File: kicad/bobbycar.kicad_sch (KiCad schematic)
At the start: 52 parts, among them J10 BREMSE, J11 CAN2, J12 PROG, J13 LED, J2 IO2, J3 GAS, J4 TFT, J5 Conn_02x08_Odd_Even, J6 Conn_02x08_Odd_Even, J7 BREMSE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

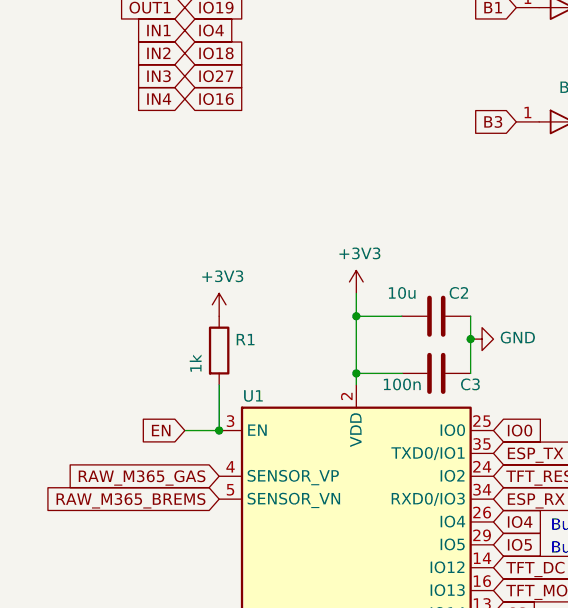
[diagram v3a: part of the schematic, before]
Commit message: Add capacitor to GND on EN
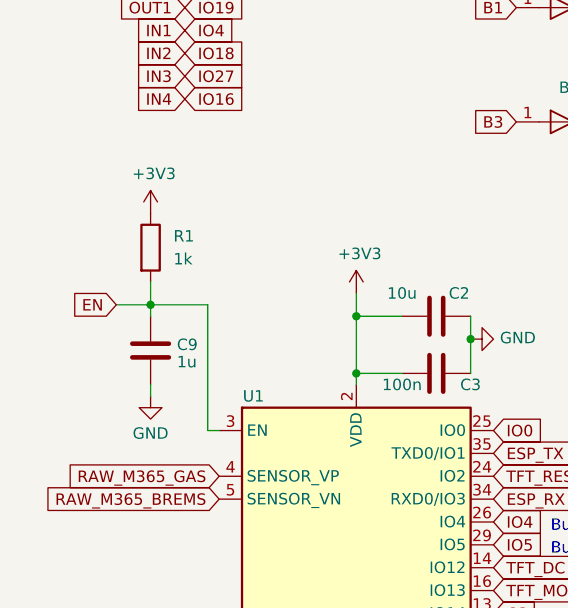
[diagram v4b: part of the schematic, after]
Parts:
- added C9: 1u, Capacitor_SMD:C_0805_2012Metric, symbol Device:C
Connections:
- net EN: now also C9.2
- net GND: now also C9.1
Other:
- moved on the sheet: R1
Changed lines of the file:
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@@
   (junction (at 109.22 170.18) (diameter 0) (color 0 0 0 0)
   )
+  (junction (at 27.94 54.61) (diameter 0) (color 0 0 0 0)
+  )
   (junction (at 350.52 102.87) (diameter 0) (color 0 0 0 0)
   )
@@
   (junction (at 115.57 39.37) (diameter 0) (color 0 0 0 0)
   )
-  (junction (at 35.56 68.58) (diameter 0) (color 0 0 0 0)
-  )
   (junction (at 391.16 95.25) (diameter 0) (color 0 0 0 0)
   )
@@
     (stroke (width 0) (type default))
   )
+  (wire (pts (xy 34.29 54.61) (xy 34.29 68.58))
+    (stroke (width 0) (type default))
+  )
   (wire (pts (xy 63.5 58.42) (xy 63.5 55.88))
     (stroke (width 0) (type default))
@@
     (stroke (width 0) (type default))
   )
+  (wire (pts (xy 34.29 68.58) (xy 35.56 68.58))
+    (stroke (width 0) (type default))
+  )
   (wire (pts (xy 120.65 170.18) (xy 109.22 170.18))
     (stroke (width 0) (type default))
@@
     (stroke (width 0) (type default))
   )
+  (wire (pts (xy 27.94 54.61) (xy 34.29 54.61))
+    (stroke (width 0) (type default))
+  )
   (wire (pts (xy 55.88 62.23) (xy 50.8 62.23))
     (stroke (width 0) (type default))
   )
+  (wire (pts (xy 27.94 63.5) (xy 27.94 64.77))
+    (stroke (width 0) (type default))
+  )
   (wire (pts (xy 161.29 107.95) (xy 156.21 107.95))
     (stroke (width 0) (type default))
   )
-  (wire (pts (xy 31.75 68.58) (xy 35.56 68.58))
+  (wire (pts (xy 24.13 54.61) (xy 27.94 54.61))
     (stroke (width 0) (type default))
   )
@@
     (stroke (width 0) (type default))
   )
+  (wire (pts (xy 27.94 54.61) (xy 27.94 55.88))
+    (stroke (width 0) (type default))
+  )
   (wire (pts (xy 57.15 182.88) (xy 72.39 182.88))
     (stroke (width 0) (type default))
   )
-  (wire (pts (xy 35.56 68.58) (xy 35.56 63.5))
+  (wire (pts (xy 27.94 54.61) (xy 27.94 52.07))
     (stroke (width 0) (type default))
   )
@@
     )
   )
-  (global_label "EN" (shape input) (at 31.75 68.58 180) (fields_autoplaced)
+  (global_label "EN" (shape input) (at 24.13 54.61 180) (fields_autoplaced)
     (effects (font (size 1.27 1.27)) (justify right))
-    (property "Intersheetrefs" "${INTERSHEET_REFS}" (at 0 0 0)
+    (property "Intersheetrefs" "${INTERSHEET_REFS}" (at -7.62 -13.97 0)
       (effects (font (size 1.27 1.27)) hide)
     )
-    (property "Referenzen zwischen Schaltplänen" "${INTERSHEET_REFS}" (at 0 0 0)
+    (property "Referenzen zwischen Schaltplänen" "${INTERSHEET_REFS}" (at -7.62 -13.97 0)
       (effects (font (size 1.27 1.27)) hide)
     )
@@
     )
   )
-  (symbol (lib_id "Device:R") (at 35.56 59.69 0) (unit 1)
+  (symbol (lib_id "Device:R") (at 27.94 48.26 0) (unit 1)
     (in_bom yes) (on_board yes) (dnp no)
-    (property "Reference" "R1" (at 37.338 58.5216 0)
+    (property "Reference" "R1" (at 30.48 46.99 0)
       (effects (font (size 1.27 1.27)) (justify left))
     )
-    (property "Value" "1k" (at 33.02 62.23 90)
+    (property "Value" "1k" (at 30.48 49.53 0)
       (effects (font (size 1.27 1.27)) (justify left))
     )
-    (property "Footprint" "Resistor_SMD:R_0603_1608Metric" (at 33.782 59.69 90)
+    (property "Footprint" "Resistor_SMD:R_0603_1608Metric" (at 26.162 48.26 90)
       (effects (font (size 1.27 1.27)) hide)
     )
-    (property "Datasheet" "~" (at 35.56 59.69 0)
+    (property "Datasheet" "~" (at 27.94 48.26 0)
       (effects (font (size 1.27 1.27)) hide)
     )
-    (property "LCSC Part #" "C21190" (at 35.56 59.69 0)
+    (property "LCSC Part #" "C21190" (at 27.94 48.26 0)
       (effects (font (size 1.27 1.27)) hide)
     )
@@
     )
   )
-  (symbol (lib_id "power:+3V3") (at 35.56 55.88 0) (unit 1)
+  (symbol (lib_id "power:+3V3") (at 27.94 44.45 0) (unit 1)
     (in_bom yes) (on_board yes) (dnp no)
-    (property "Reference" "#PWR01" (at 35.56 59.69 0)
+    (property "Reference" "#PWR01" (at 27.94 48.26 0)
       (effects (font (size 1.27 1.27)) hide)
     )
-    (property "Value" "+3V3" (at 35.941 51.4858 0)
+    (property "Value" "+3V3" (at 28.321 40.0558 0)
       (effects (font (size 1.27 1.27)))
     )
-    (property "Footprint" "" (at 35.56 55.88 0)
+    (property "Footprint" "" (at 27.94 44.45 0)
       (effects (font (size 1.27 1.27)) hide)
     )
-    (property "Datasheet" "" (at 35.56 55.88 0)
+    (property "Datasheet" "" (at 27.94 44.45 0)
       (effects (font (size 1.27 1.27)) hide)
     )
@@
     )
   )
+  (symbol (lib_id "power:GND") (at 27.94 64.77 0) (unit 1)
+    (in_bom yes) (on_board yes) (dnp no) (fields_autoplaced)
+    (property "Reference" "#PWR023" (at 27.94 71.12 0)
+      (effects (font (size 1.27 1.27)) hide)
+    )
+    (property "Value" "GND" (at 27.94 68.9055 0)
+      (effects (font (size 1.27 1.27)))
+    )
+    (property "Footprint" "" (at 27.94 64.77 0)
+      (effects (font (size 1.27 1.27)) hide)
+    )
+    (property "Datasheet" "" (at 27.94 64.77 0)
+      (effects (font (size 1.27 1.27)) hide)
+    )
+    (pin "1")
+    (instances
+      (project "bobbycar"
+        (path "/477311b9-8f81-40c8-9c55-fd87e287247a"
+          (reference "#PWR023") (unit 1)
+        )
+      )
+    )
+  )
   (symbol (lib_id "power:GND") (at 212.09 -48.26 0) (unit 1)
     (in_bom yes) (on_board yes) (dnp no)
@@
         )
       )
+    )
+  )
+  (symbol (lib_id "Device:C") (at 27.94 59.69 180) (unit 1)
+    (in_bom yes) (on_board yes) (dnp no) (fields_autoplaced)
+    (property "Reference" "C9" (at 30.861 59.0463 0)
+      (effects (font (size 1.27 1.27)) (justify right))
+    )
+    (property "Value" "1u" (at 30.861 60.9673 0)
+      (effects (font (size 1.27 1.27)) (justify right))
+    )
+    (property "Footprint" "Capacitor_SMD:C_0805_2012Metric" (at 26.9748 55.88 0)
+      (effects (font (size 1.27 1.27)) hide)
+    )
+    (property "Datasheet" "~" (at 27.94 59.69 0)
+      (effects (font (size 1.27 1.27)) hide)
+    )
+    (property "LCSC Part #" "C28323" (at 27.94 59.69 90)
+      (effects (font (size 1.27 1.27)) hide)
+    )
+    (pin "1")
+    (pin "2")
+    (instances
+      (project "bobbycar"
+        (path "/477311b9-8f81-40c8-9c55-fd87e287247a"
+          (reference "C9") (unit 1)
+        )
+        (path "/477311b9-8f81-40c8-9c55-fd87e287247a/fb6a09a0-59ad-4d19-a51f-8816d804aa4a"
+          (reference "C10") (unit 1)
+        )
+      )

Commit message: Use proper symbols instead of labels for GND and +15V
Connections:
- net 15V renamed +15V
